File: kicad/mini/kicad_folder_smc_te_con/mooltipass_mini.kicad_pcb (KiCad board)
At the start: 2 copper layers, 74.9 x 32.5 mm, 65 parts, among them CON1 CON_10118194-0001LF, P1 EMC, P2 EMC, P3 EMC, P4 EMC, Q1 MOS_P, Q2 MOS_N, Q3 MOS_P, Q4 MOS_N, U1 IP4234CZ6,125, U2 ST662ACD, U3 CON_UGM128032A6B01, U4 CON_SMARTCARD2, U5 AT45DB011D, U6 ATMEGA32U4_QFN, U7 LIS2HH12, U8 TS005_WHEEL_CLICK, X1 16MHz

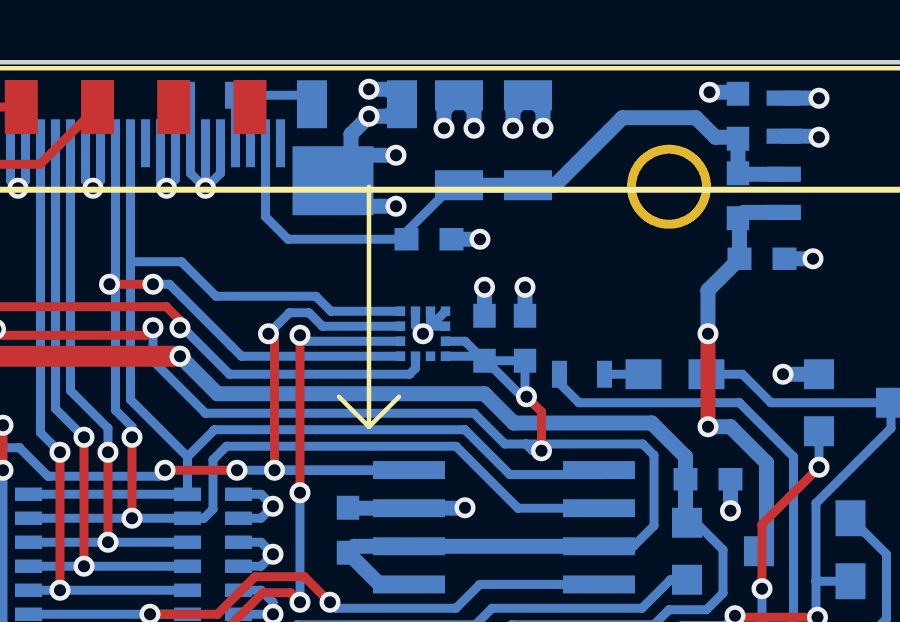
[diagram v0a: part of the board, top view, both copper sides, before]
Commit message: final gerbers for mini with chinese card connector clone
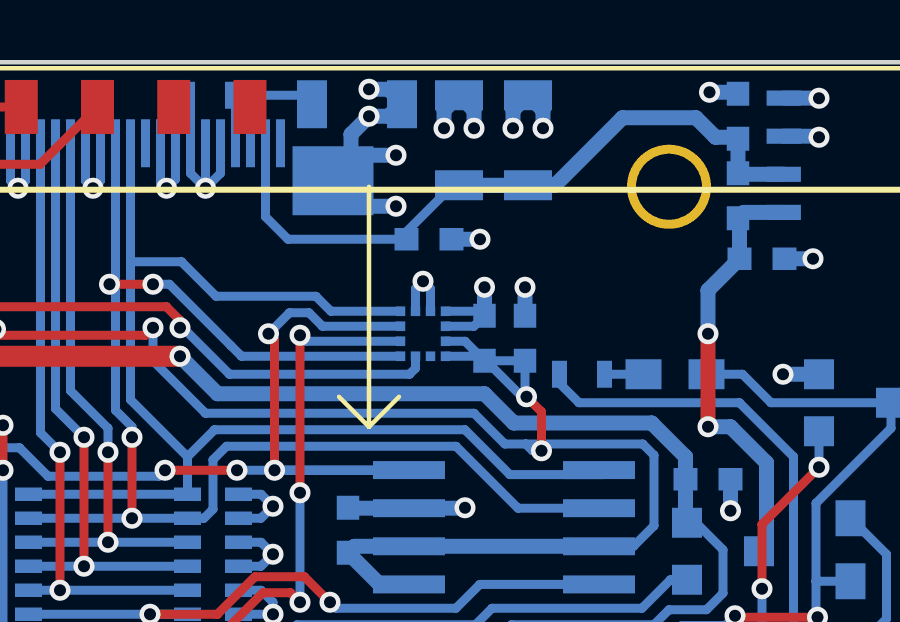
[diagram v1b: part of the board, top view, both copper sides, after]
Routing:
- net GND: track 199.2 -> 200.9 mm
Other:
- board text added: "Mooltipass Mini by Stephan Electronics Licensed under CERN OHL V1.2 v5"
- board text removed: "Mooltipass Mini by Stephan Electronics Licensed under CERN OHL V1.2 v4"
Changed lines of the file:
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@@
     (thickness 1.6)
     (drawings 23)
-    (tracks 860)
+    (tracks 861)
     (zones 0)
     (modules 65)
@@
   (page A4)
   (layers
-    (0 F.Cu signal)
+    (0 F.Cu signal hide)
     (31 B.Cu signal)
     (32 B.Adhes user)
@@
   (gr_line (start 123.75 99.5) (end 123.75 74.7) (angle 90) (layer Eco2.User) (width 0.2))
   (gr_arc (start 101 99) (end 101 100) (angle 90) (layer Edge.Cuts) (width 0.15))
-  (gr_text "Mooltipass Mini by Stephan Electronics\nLicensed under CERN OHL V1.2\nv4" (at 149.15 95) (layer B.SilkS)
+  (gr_text "Mooltipass Mini by Stephan Electronics\nLicensed under CERN OHL V1.2\nv5" (at 149.15 95) (layer B.SilkS)
     (effects (font (size 1.3 1.3) (thickness 0.3)) (justify mirror))
   )
@@
   (segment (start 153.525 72.505) (end 152.195 72.505) (width 0.5) (layer B.Cu) (net 2) (status 30))
   (segment (start 152.195 72.505) (end 152 72.7) (width 0.5) (layer B.Cu) (net 2) (status 30))
+  (segment (start 142.25 75.8) (end 143.4 75.8) (width 0.3) (layer B.Cu) (net 3) (status C00000))
+  (segment (start 143.4 75.8) (end 143.55 75.95) (width 0.3) (layer B.Cu) (net 3) (status C00000))
+  (segment (start 142.25 76.3) (end 143.2 76.3) (width 0.3) (layer B.Cu) (net 3) (status C00000))
+  (segment (start 143.2 76.3) (end 143.55 75.95) (width 0.3) (layer B.Cu) (net 3) (status C00000))
+  (segment (start 141.75 75.8) (end 141.75 75.05) (width 0.3) (layer B.Cu) (net 3) (status 400000))
+  (segment (start 141.25 75.05) (end 141.5 74.8) (width 0.3) (layer B.Cu) (net 3))
+  (via (at 141.5 74.8) (size 0.7) (drill 0.4) (layers F.Cu B.Cu) (net 3))
+  (segment (start 141.25 75.05) (end 141.25 75.8) (width 0.3) (layer B.Cu) (net 3) (status 800000))
+  (segment (start 141.75 75.05) (end 141.5 74.8) (width 0.3) (layer B.Cu) (net 3))
   (segment (start 107.95 88.7) (end 107 88.7) (width 0.3) (layer B.Cu) (net 3))
   (via (at 107 88.7) (size 0.7) (drill 0.4) (layers F.Cu B.Cu) (net 3))
@@
   (segment (start 143.55 75.95) (end 143.55 75) (width 0.5) (layer B.Cu) (net 3))
   (via (at 143.55 75) (size 0.7) (drill 0.4) (layers F.Cu B.Cu) (net 3))
-  (segment (start 142.25 75.8) (end 141.75 76.3) (width 0.3) (layer B.Cu) (net 3))
-  (segment (start 142.25 76.3) (end 141.75 76.3) (width 0.3) (layer B.Cu) (net 3))
-  (segment (start 141.75 76.3) (end 141.5 76.55) (width 0.3) (layer B.Cu) (net 3))
-  (segment (start 141.25 75.8) (end 141.25 76.3) (width 0.3) (layer B.Cu) (net 3))
-  (segment (start 141.75 76.3) (end 141.5 76.55) (width 0.3) (layer B.Cu) (net 3))
-  (via (at 141.5 76.55) (size 0.7) (drill 0.4) (layers F.Cu B.Cu) (net 3))
-  (segment (start 141.75 76.3) (end 141.75 75.8) (width 0.3) (layer B.Cu) (net 3))
-  (segment (start 141.25 76.3) (end 141.5 76.55) (width 0.3) (layer B.Cu) (net 3))
   (segment (start 135.35 85.1) (end 136.1 85.1) (width 0.3) (layer B.Cu) (net 3) (status 10))
   (via (at 136.5 85.9) (size 0.7) (drill 0.4) (layers F.Cu B.Cu) (net 3))
